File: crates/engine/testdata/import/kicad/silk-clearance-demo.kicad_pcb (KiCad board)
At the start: 2 copper layers, 0 parts

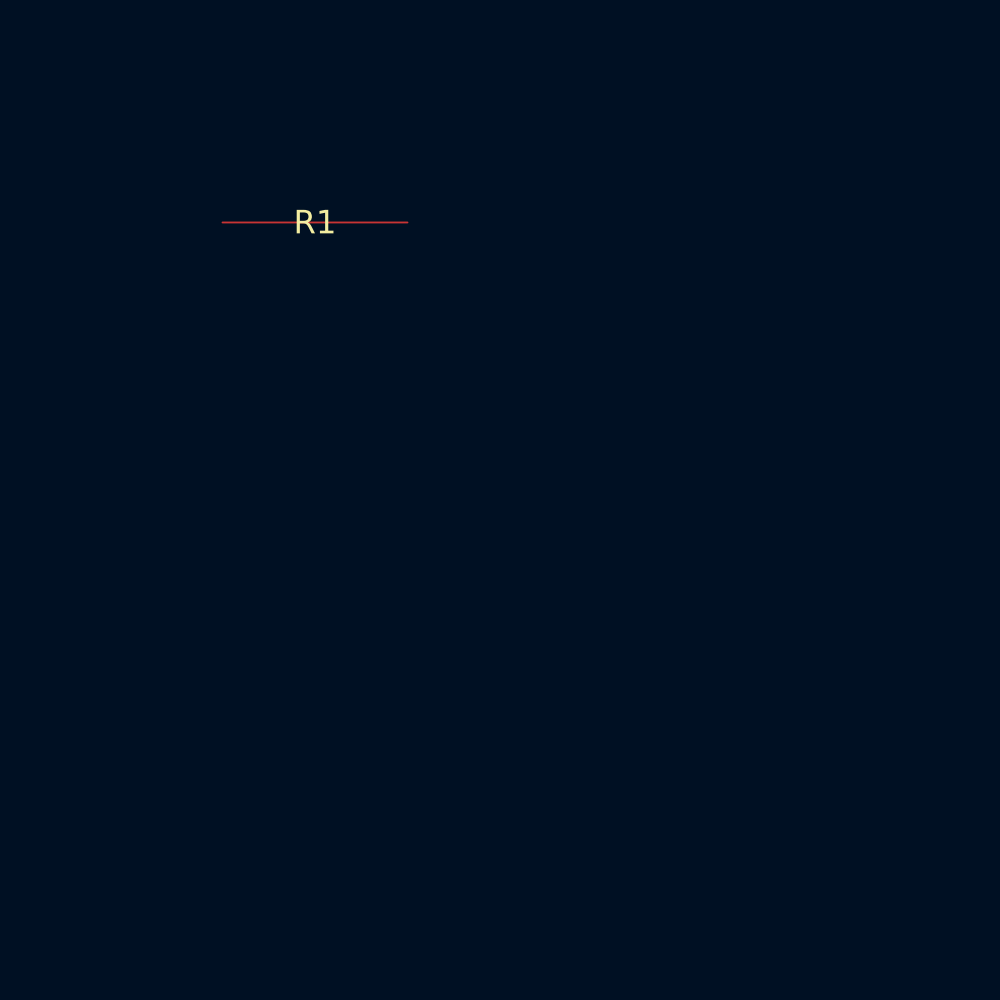
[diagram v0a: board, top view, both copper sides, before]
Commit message: M7: imported-board fidelity track and KiCad import depth
Opens the post-spike imported-board fidelity correction track inside the
opening M7 milestone. PROGRESS and m7_opening now record the delivery
rule, standards amendment, and acceptance checks for import / scene /
renderer fidelity; PLAN re-sequences the opening slice accordingly.

Engine / import:
- KiCad import gains footprint, layer, pad-fallback, pad-layer, and
  pad-rotation test modules and corresponding skeleton/parser growth.
- board pad/net_graph/board_info carry the fidelity-facing shape and
  net-semantics changes; DRC and export tests absorb the new invariants.
- CLI project/board command surfaces track the expanded engine API.

GUI crates:
- gui-protocol, gui-render, and gui-app build out the review-workspace
  scene contract, semantic render lanes, and locked shell needed to
  stand up imported-board review on top of the closed M5 substrate.

Docs:
- New M7 guidance set: delivery gates, imported-board fidelity plan /
  checklist / fixtures / artifacts / issues, render semantic contract,
  layer-discipline memo, airwire and copper rendering guidance, and
  IMP briefs/decisions (layer fallback, outline ownership, pad rotation,
  pad layer identity, edge-cuts layer fidelity).
- Adds IPC_FOOTPRINT_SYSTEM and STANDARDS_COMPLIANCE_INTEGRATION_GUIDANCE.
- scripts/datum_assistant_bridge.py: read-only assistant bridge used by
  the review shell; no engine authority, schema-constrained actions only.
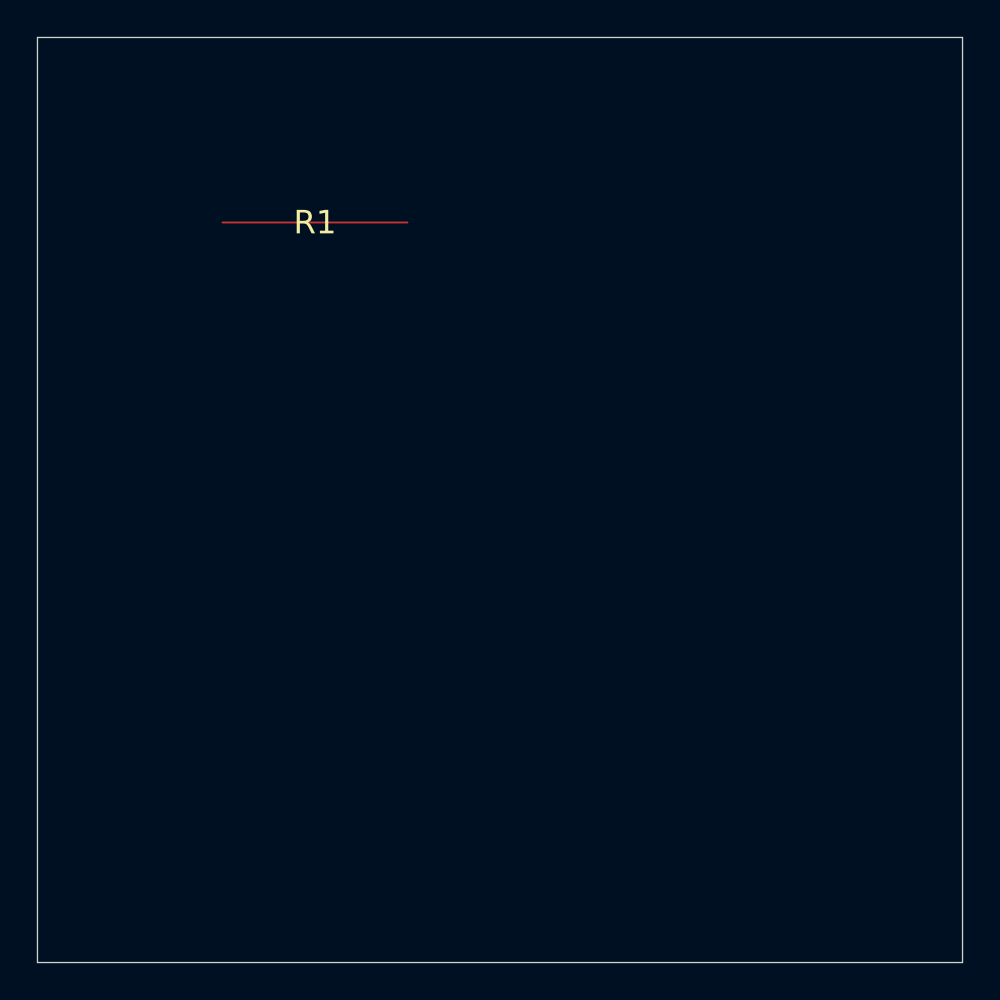
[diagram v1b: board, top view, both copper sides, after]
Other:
- board outline added: 50 x 50 mm
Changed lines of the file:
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@@
     (at 15 10 0)
     (layer "F.SilkS")
+)
+  (gr_line
+    (start 0 0)
+    (end 50 0)
+    (stroke (width 0.05) (type solid))
+    (layer "Edge.Cuts")
+)
+  (gr_line
+    (start 50 0)
+    (end 50 50)
+    (stroke (width 0.05) (type solid))
+    (layer "Edge.Cuts")
+)
+  (gr_line
+    (start 50 50)
+    (end 0 50)
+    (stroke (width 0.05) (type solid))
+    (layer "Edge.Cuts")
+)
+  (gr_line
+    (start 0 50)
+    (end 0 0)
+    (stroke (width 0.05) (type solid))
+    (layer "Edge.Cuts")
 ))
